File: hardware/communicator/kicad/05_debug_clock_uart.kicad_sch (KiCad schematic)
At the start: 13 parts, among them J10 SWD 2x5 1.27mm, Y1 ABM8-16.000MHZ-B2-T

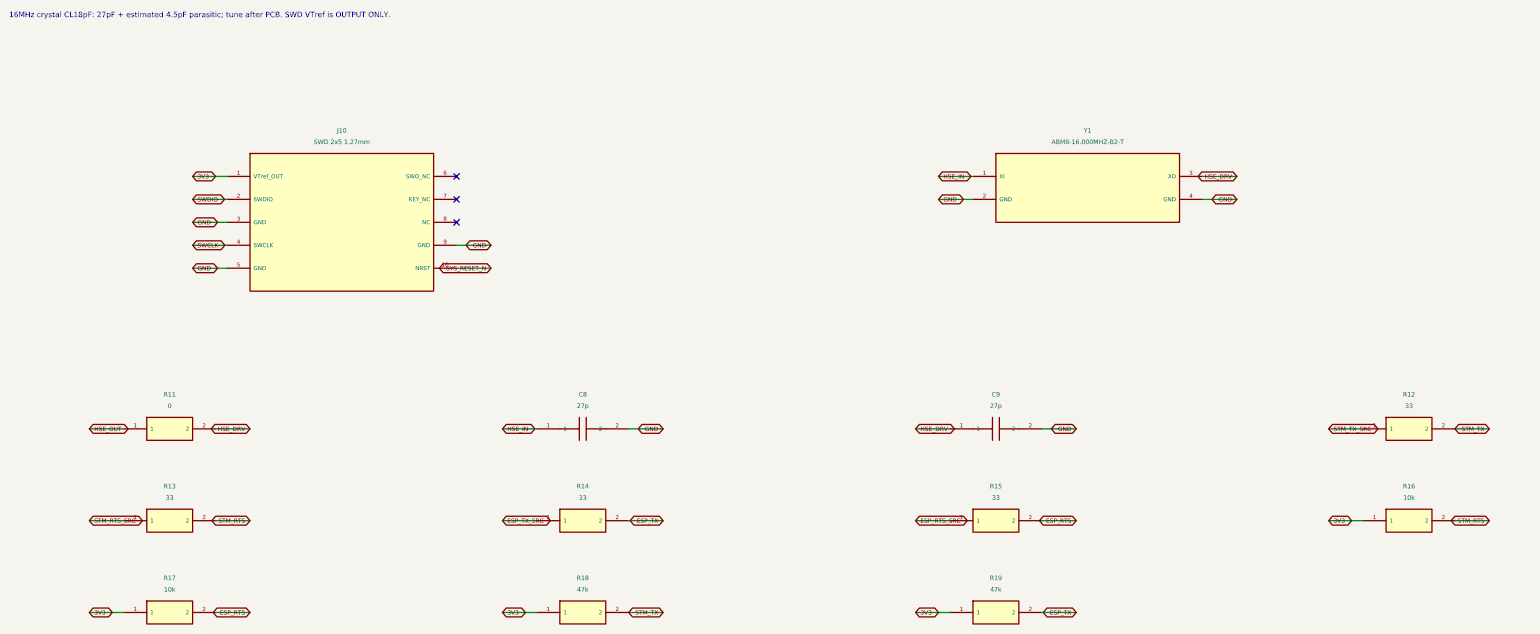
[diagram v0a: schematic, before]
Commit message: feat: add R1 detailed hardware and navigation protocol review candidate
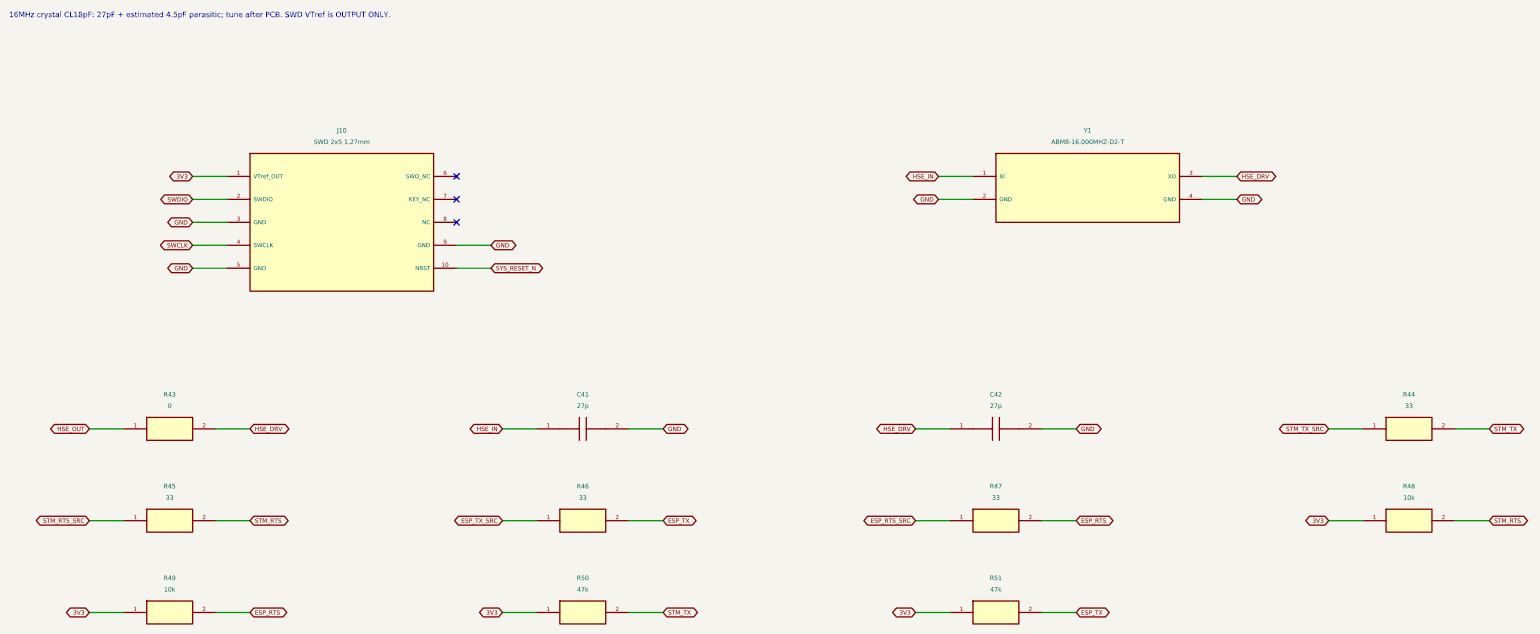
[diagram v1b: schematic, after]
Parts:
- removed C8: 27p, CANView:Capacitor_SMD__C_0402_1005Metric, symbol CANView:CANView_communicator_C8
- removed C9: 27p, CANView:Capacitor_SMD__C_0402_1005Metric, symbol CANView:CANView_communicator_C9
- removed R11: 0, CANView:Resistor_SMD__R_0402_1005Metric, symbol CANView:CANView_communicator_R11
- removed R12: 33, CANView:Resistor_SMD__R_0402_1005Metric, symbol CANView:CANView_communicator_R12
- removed R13: 33, CANView:Resistor_SMD__R_0402_1005Metric, symbol CANView:CANView_communicator_R13
- removed R14: 33, CANView:Resistor_SMD__R_0402_1005Metric, symbol CANView:CANView_communicator_R14
- removed R15: 33, CANView:Resistor_SMD__R_0402_1005Metric, symbol CANView:CANView_communicator_R15
- removed R16: 10k, CANView:Resistor_SMD__R_0402_1005Metric, symbol CANView:CANView_communicator_R16
- removed R17: 10k, CANView:Resistor_SMD__R_0402_1005Metric, symbol CANView:CANView_communicator_R17
- removed R18: 47k, CANView:Resistor_SMD__R_0402_1005Metric, symbol CANView:CANView_communicator_R18
- removed R19: 47k, CANView:Resistor_SMD__R_0402_1005Metric, symbol CANView:CANView_communicator_R19
- added C41: 27p, CANView:Capacitor_SMD__C_0402_1005Metric, symbol CANView:CANView_communicator_C41
- added C42: 27p, CANView:Capacitor_SMD__C_0402_1005Metric, symbol CANView:CANView_communicator_C42
- added R43: 0, CANView:Resistor_SMD__R_0402_1005Metric, symbol CANView:CANView_communicator_R43
- added R44: 33, CANView:Resistor_SMD__R_0402_1005Metric, symbol CANView:CANView_communicator_R44
- added R45: 33, CANView:Resistor_SMD__R_0402_1005Metric, symbol CANView:CANView_communicator_R45
- added R46: 33, CANView:Resistor_SMD__R_0402_1005Metric, symbol CANView:CANView_communicator_R46
- added R47: 33, CANView:Resistor_SMD__R_0402_1005Metric, symbol CANView:CANView_communicator_R47
- added R48: 10k, CANView:Resistor_SMD__R_0402_1005Metric, symbol CANView:CANView_communicator_R48
- added R49: 10k, CANView:Resistor_SMD__R_0402_1005Metric, symbol CANView:CANView_communicator_R49
- added R50: 47k, CANView:Resistor_SMD__R_0402_1005Metric, symbol CANView:CANView_communicator_R50
- added R51: 47k, CANView:Resistor_SMD__R_0402_1005Metric, symbol CANView:CANView_communicator_R51
- J10: Specification Keyed shrouded matching cable required; VTref sense only, n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 -> Unshrouded header; matching keyed adapter or controlled pin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
- Y1: value ABM8-16.000MHZ-B2-T -> ABM8-16.000MHZ-D2-T; MPN ABM8-16.000MHZ-B2-T -> ABM8-16.000MHZ-D2-T; Source abracon-abm8 -> abracon-abm8: pp1-2, D temperature option; Specification 16MHz; CL18pF; ±20ppm; ±50ppm temperature; ESR80ohm maximum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 -> 16MHz; CL18pF; ±20ppm; ±50ppm temperature; -40..85C; ESR70o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
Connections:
- net 3V3: now also R48.1, R49.1, R50.1, R51.1
- net ESP_RTS: now also R47.2, R49.2
- net ESP_RTS_SRC: now also R47.1
- net ESP_TX: now also R46.2, R51.2
- net ESP_TX_SRC: now also R46.1
- net GND: now also C41.2, C42.2
- net HSE_DRV: now also C42.1, R43.2
- net HSE_IN: now also C41.1
- net HSE_OUT: now also R43.1
- net STM_RTS: now also R45.2, R48.2
- net STM_RTS_SRC: now also R45.1
- net STM_TX: now also R44.2, R50.2
- net STM_TX_SRC: now also R44.1

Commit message: fix: close hardware rail-fault paths and sensor contract gaps
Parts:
- removed C41: 27p, CANView:Capacitor_SMD__C_0402_1005Metric, symbol CANView:CANView_communicator_C41
- removed C42: 27p, CANView:Capacitor_SMD__C_0402_1005Metric, symbol CANView:CANView_communicator_C42
- removed R43: 0, CANView:Resistor_SMD__R_0402_1005Metric, symbol CANView:CANView_communicator_R43
- added C43: 27p, CANView:Capacitor_SMD__C_0402_1005Metric, symbol CANView:CANView_communicator_C43
- added C44: 27p, CANView:Capacitor_SMD__C_0402_1005Metric, symbol CANView:CANView_communicator_C44
- added R52: 47k, CANView:Resistor_SMD__R_0402_1005Metric, symbol CANView:CANView_communicator_R52
- R44: value 33 -> 0; MPN GEN-R-0402-33-1% -> GEN-R-0402-0-1%
- R48: value 10k -> 33; MPN GEN-R-0402-10k-1% -> GEN-R-0402-33-1%
- R50: value 47k -> 10k; MPN GEN-R-0402-47k-1% -> GEN-R-0402-10k-1%
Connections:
- net 3V3: now also R52.1; no longer R48.1
- net ESP_RTS: now also R48.2, R50.2; no longer R47.2, R49.2
- net ESP_RTS_SRC: now also R48.1; no longer R47.1
- net ESP_TX: now also R47.2, R52.2; no longer R46.2, R51.2
- net ESP_TX_SRC: now also R47.1; no longer R46.1
- net GND: now also C43.2, C44.2
- net HSE_DRV: now also R44.2, C44.1
- net HSE_IN: now also C43.1
- net HSE_OUT: now also R44.1
- net STM_RTS: now also R46.2, R49.2; no longer R45.2, R48.2
- net STM_RTS_SRC: now also R46.1; no longer R45.1
- net STM_TX: now also R45.2, R51.2; no longer R44.2, R50.2
- net STM_TX_SRC: now also R45.1; no longer R44.1
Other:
- moved on the sheet: R44, R45, R46, R47, R48, R49, R50, R51

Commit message: Design independent OTA recovery and update N16R8 hardware
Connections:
- net SYS_RESET_N renamed STM_RESET_N
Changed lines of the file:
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@@
 (global_label "GND" (shape bidirectional) (at 121.9200 66.0400 0) (effects (font (size 0.95 0.95)) (justify left)) (property "Intersheetrefs" "${INTERSHEET_REFS}" (at 121.9200 66.0400 0) (hide yes) (effects (font (size 1.0 1.0)) )))
 (wire (pts (xy 114.3000 71.1200) (xy 121.9200 71.1200)) (stroke (width 0) (type default)))
-(global_label "SYS_RESET_N" (shape bidirectional) (at 121.9200 71.1200 0) (effects (font (size 0.95 0.95)) (justify left)) (property "Intersheetrefs" "${INTERSHEET_REFS}" (at 121.9200 71.1200 0) (hide yes) (effects (font (size 1.0 1.0)) )))
+(global_label "STM_RESET_N" (shape bidirectional) (at 121.9200 71.1200 0) (effects (font (size 0.95 0.95)) (justify left)) (property "Intersheetrefs" "${INTERSHEET_REFS}" (at 121.9200 71.1200 0) (hide yes) (effects (font (size 1.0 1.0)) )))
 (symbol (lib_id "CANView:CANView_communicator_R45") (at 325.1200 106.6800 0) (unit 1) (in_bom yes) (on_board yes) (dnp no) (property "Reference" "R45" (at 325.1200 99.0600 0)  (effects (font (size 1.0 1.0)) ))(property "Value" "33" (at 325.1200 101.6000 0)  (effects (font (size 1.0 1.0)) ))(property "Footprint" "CANView:Resistor_SMD__R_0402_1005Metric" (at 325.1200 106.6800 0) (hide yes) (effects (font (size 1.0 1.0)) ))(property "MPN" "GEN-R-0402-33-1%" (at 325.1200 106.6800 0) (hide yes) (effects (font (size 1.0 1.0)) ))(property "Specification" "0.1W; 50V; ±1%; ±100ppm/K; -55..155C" (at 325.1200 106.6800 0) (hide yes) (effects (font (size 1.0 1.0)) ))(property "Source" "" (at 325.1200 106.6800 0) (hide yes) (effects (font (size 1.0 1.0)) ))(property "Assembly" "FIT" (at 325.1200 106.6800 0) (hide yes) (effects (font (size 1.0 1.0)) ))(instances (project "communicator" (path "/c8ff26d1-0b80-520e-ae3f-45aa29bfe092/3450400d-087d-5659-b1f4-e2e471cde01d" (reference "R45") (unit 1)))))
 (wire (pts (xy 314.9600 106.6800) (xy 307.3400 106.6800)) (stroke (width 0) (type default)))
